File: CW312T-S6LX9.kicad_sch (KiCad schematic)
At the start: 0 parts

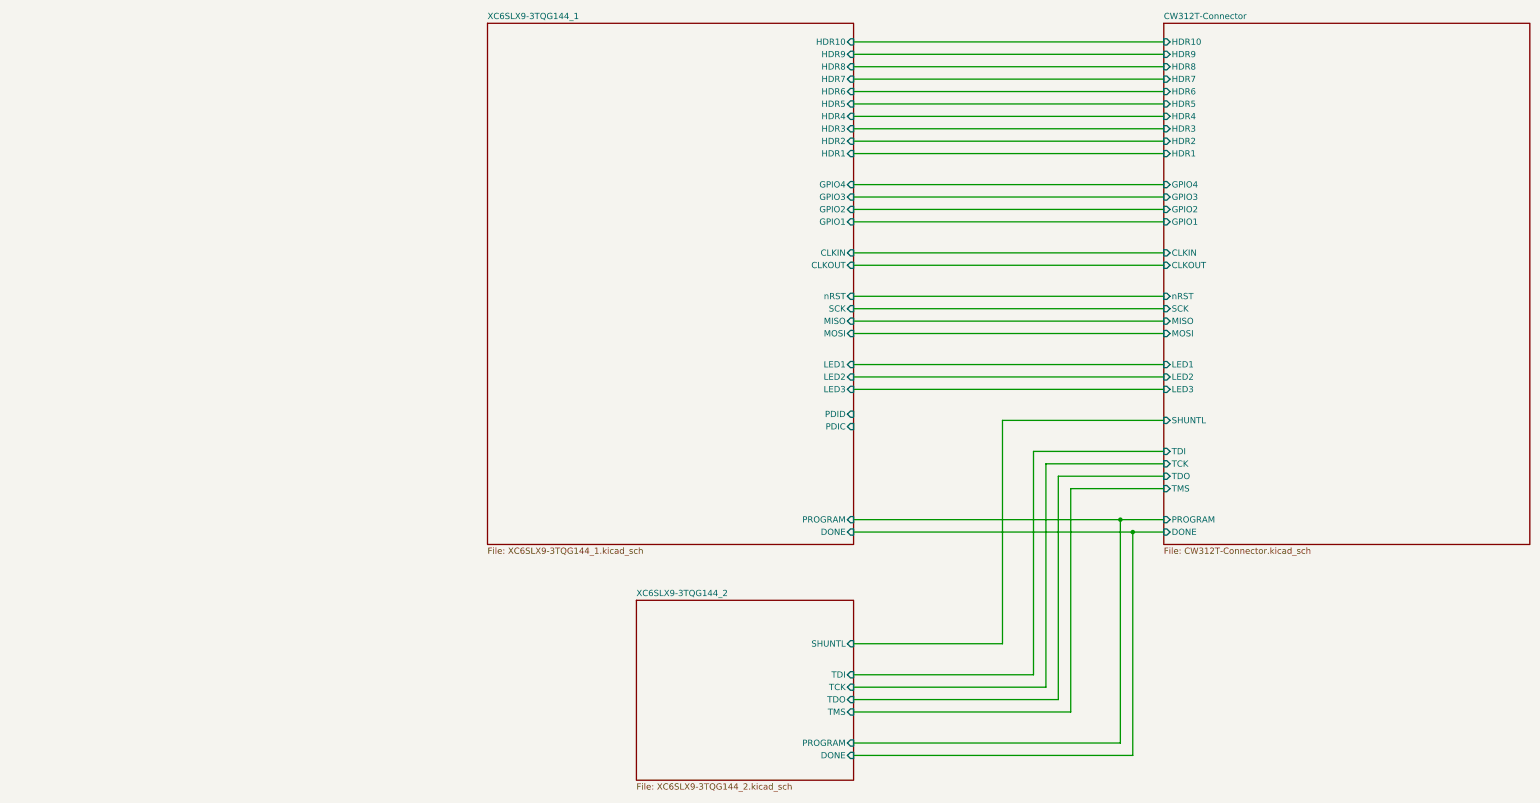
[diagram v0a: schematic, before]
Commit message: updated design - still needs vcc routing
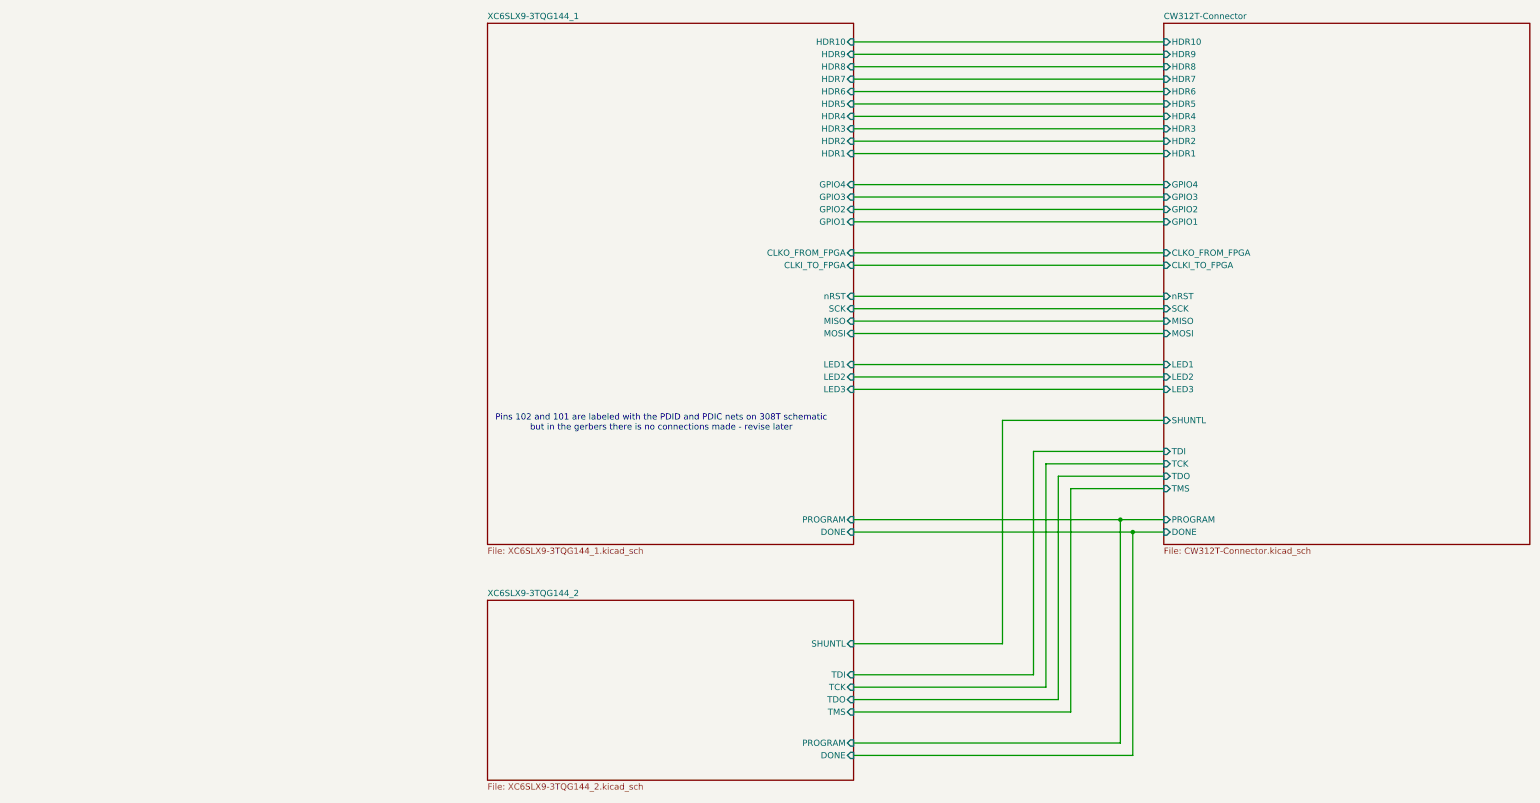
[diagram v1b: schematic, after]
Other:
- sheet CW312T-Connector ports: added CLKI_TO_FPGA, CLKO_FROM_FPGA; removed CLKIN, CLKOUT
- sheet XC6SLX9-3TQG144_1 ports: added CLKI_TO_FPGA, CLKO_FROM_FPGA; removed CLKIN, CLKOUT, PDIC, PDID
- note added: "Pins 102 and 101 are labeled with the PDID and PDIC nets on 308T schematic but in the gerbers there is no connections made - revise later"

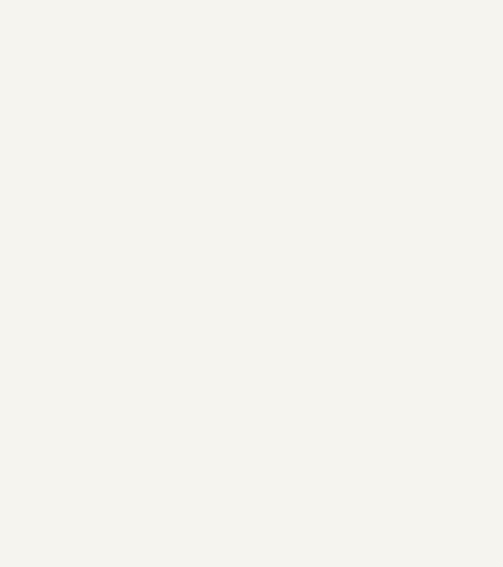
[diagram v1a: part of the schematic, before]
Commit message: added inner layers for gnd and pwr planes, added silkscreen, updated cw312t template
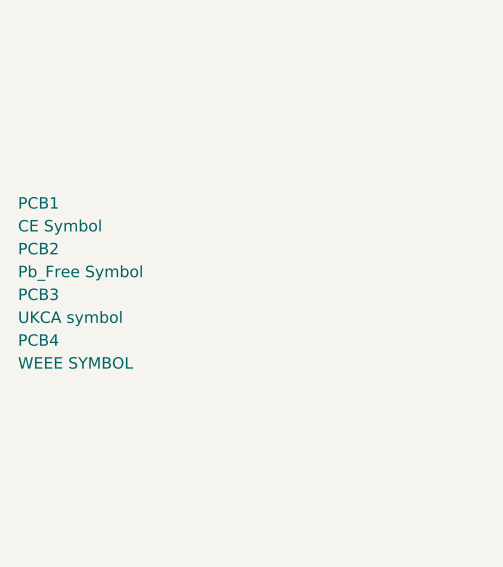
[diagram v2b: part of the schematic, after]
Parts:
- added PCB1: CE Symbol, Silkscrren_Symbols:CE-Logo_8.5x6mm_SilkScreen, symbol Silkscreen_Symbols:CE_Free
- added PCB2: Pb_Free Symbol, Silkscrren_Symbols:Pb_Free_8.0x8.0mm_SilkScreen, symbol Silkscreen_Symbols:Pb_Free
- added PCB3: UKCA symbol, Silkscrren_Symbols:UKCA-Logo_8x8mm_SilkScreen, symbol Silkscreen_Symbols:UKCA
- added PCB4: WEEE SYMBOL, Silkscrren_Symbols:WEEE-Logo_5.6x8mm_SilkScreen, symbol Silkscreen_Symbols:WEEE

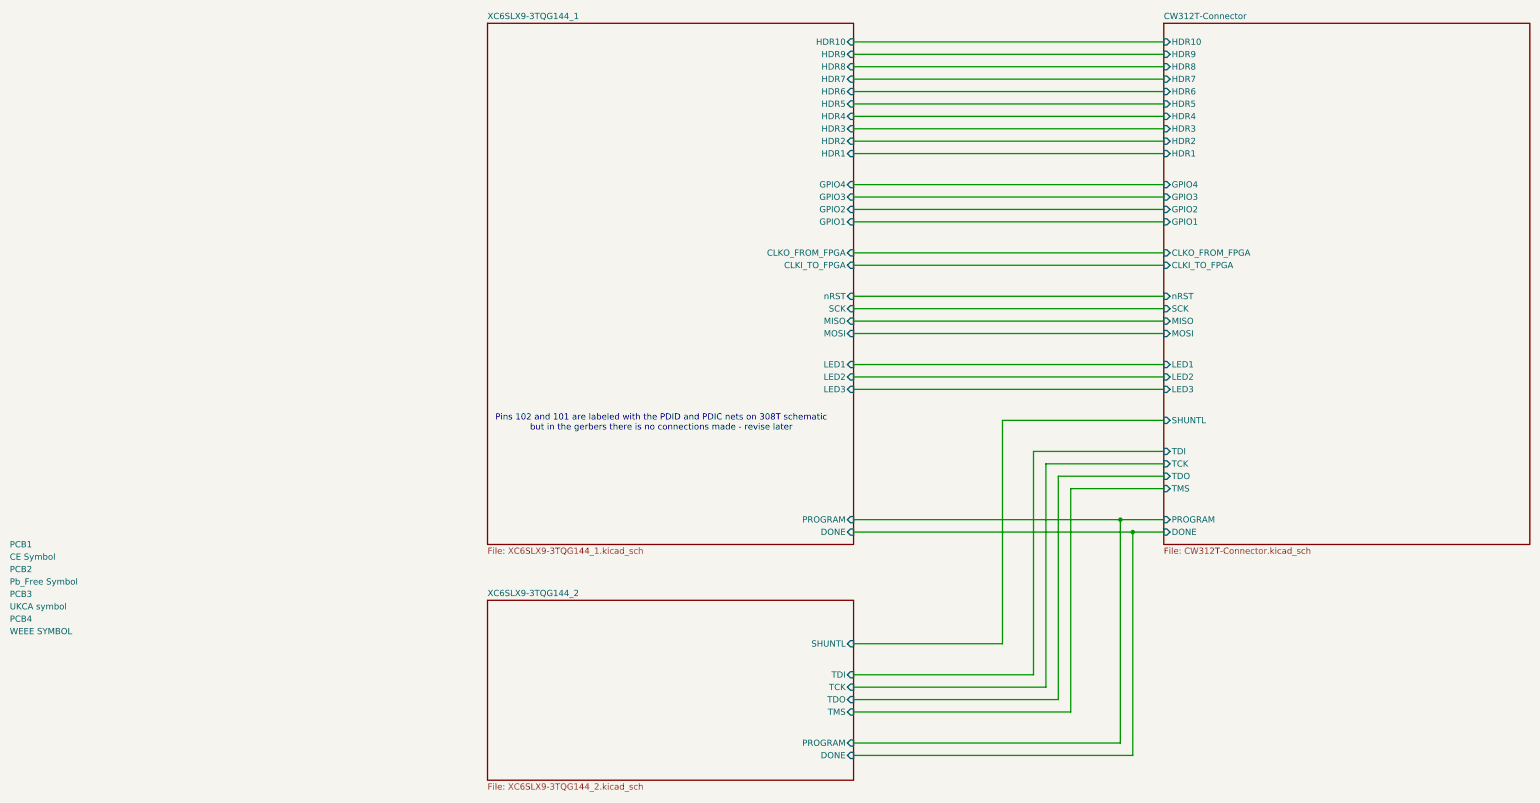
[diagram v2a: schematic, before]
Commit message: updated schematic and pcb, fixed silkscreen - Ready for review
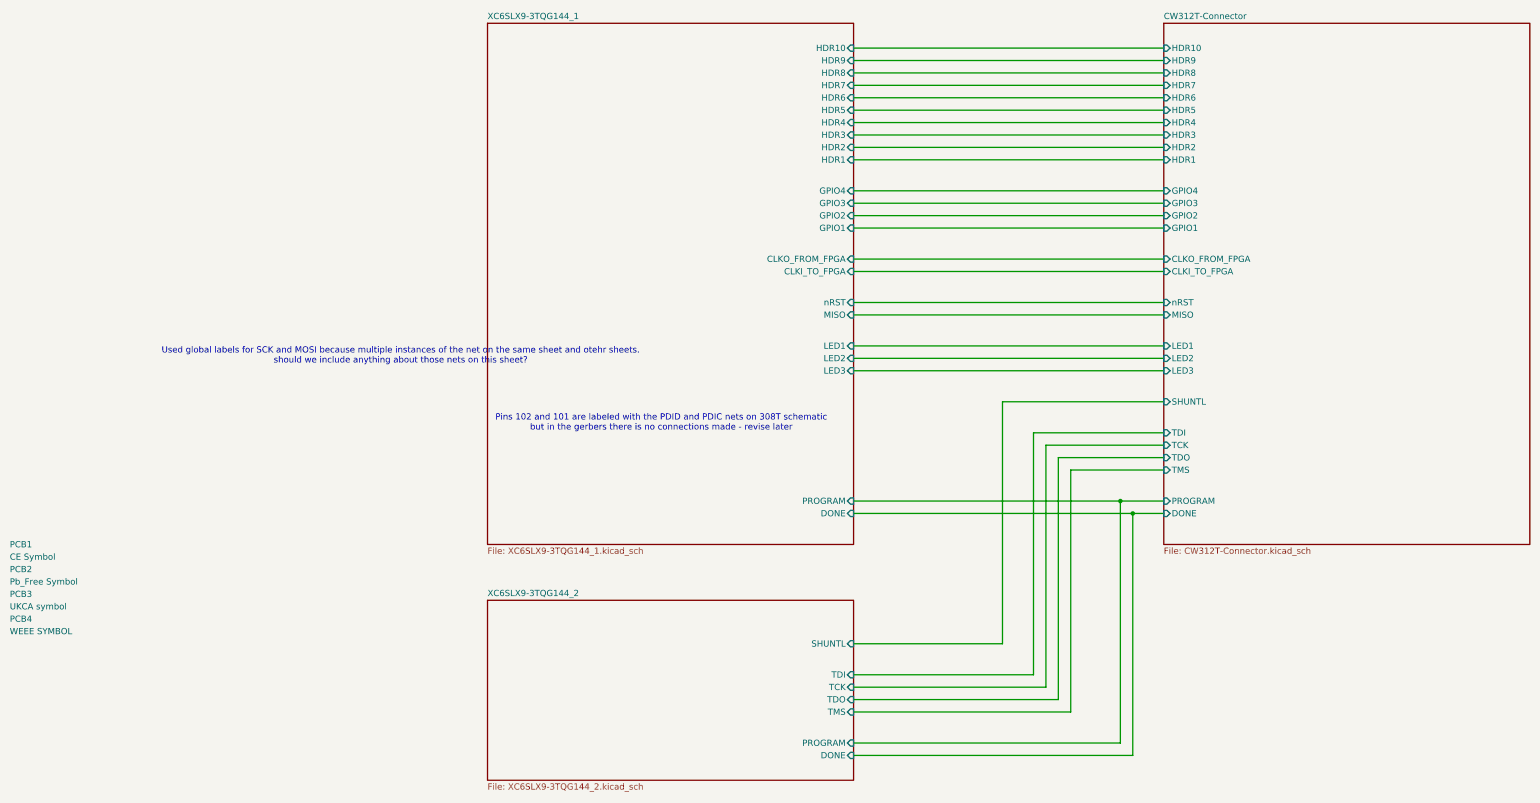
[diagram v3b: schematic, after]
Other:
- sheet CW312T-Connector ports: added none; removed MOSI, SCK
- sheet XC6SLX9-3TQG144_1 ports: added none; removed MOSI, SCK
- note added: "Used global labels for SCK and MOSI because multiple instances of the net on the same sheet and otehr sheets. should we include anything about those nets on this sheet?"
